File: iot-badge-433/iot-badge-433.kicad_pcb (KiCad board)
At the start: 2 copper layers, 70 x 100 mm, 72 parts, among them J1 USB_C_Receptacle_USB2.0, J2 Wire ANT, J3 Conn_01x04_Male, Q1 BC847, Q2 BC847, SW1 SW_Push, SW2 SW_Push, SW3 SW_Push, SW4 SW_Push, SW5 SW_Push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

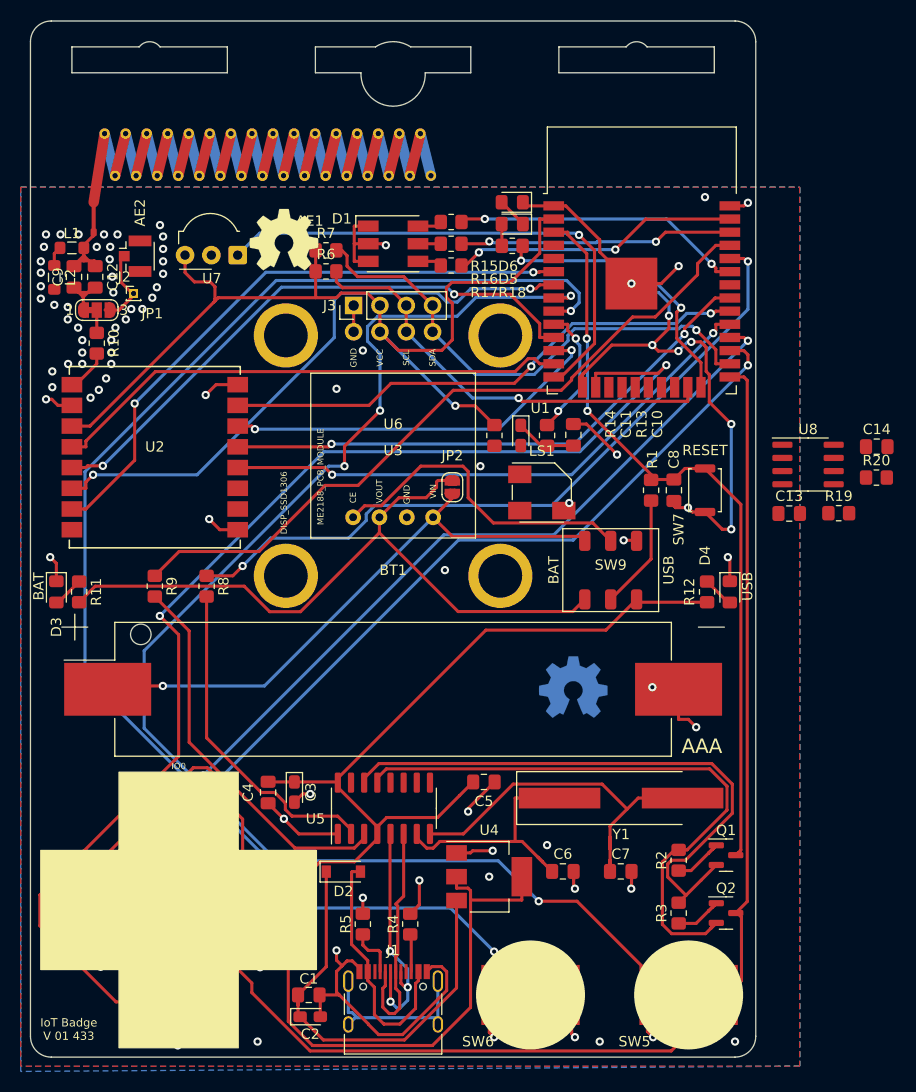
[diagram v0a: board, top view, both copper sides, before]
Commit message: audio amp elements routed
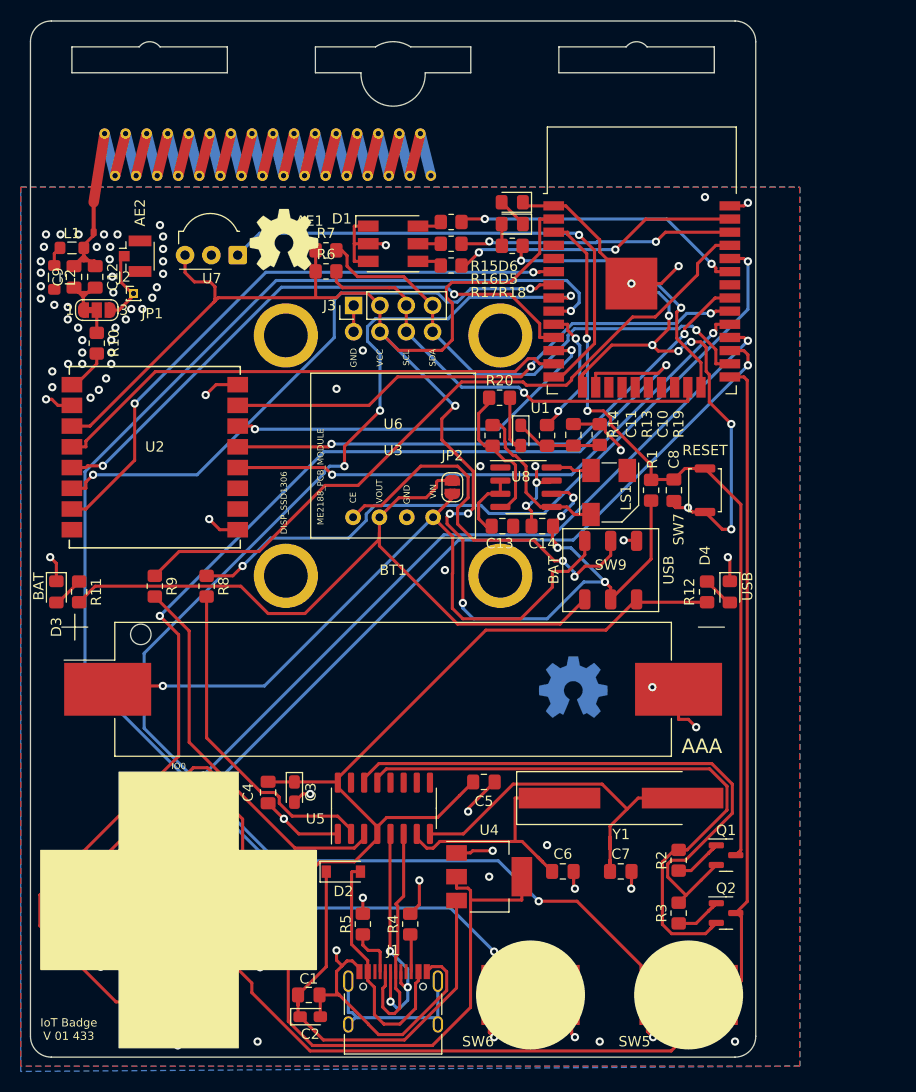
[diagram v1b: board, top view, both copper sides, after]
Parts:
- moved R20 37.2 mm to (145.3, 86.4)
- moved C14 33.2 mm to (149.4, 98.8), turned to 180 degrees
- moved C13 27.7 mm to (145.6, 98.8)
- moved U8 27.3 mm to (147.8, 95.0)
- moved R19 24.3 mm to (154.9, 89.9), turned to -90 degrees
- moved LS1 6.50 mm to (155.8, 95.5), turned to -90 degrees
- moved R14 0.18 mm to (144.6, 90.0)
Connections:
- LS1 pad 2: Net-(LS1-Pad2) -> Net-(U8-Pad8)
- LS1 pad 3: Net-(LS1-Pad3) -> Net-(R14-Pad1)
- R14 pad 1: Net-(LS1-Pad2) -> Net-(R14-Pad1)
- U8 pad 5: Net-(LS1-Pad2) -> Net-(R14-Pad1)
- U8 pad 8: Net-(LS1-Pad3) -> Net-(U8-Pad8)
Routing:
- net +3V3: track 103.3 -> 154.5 mm, vias 1 -> 8
- net Net-(R14-Pad1): track 0.00 -> 15.6 mm
- net Net-(R14-Pad2): track 0.00 -> 14.2 mm
- net +BATT: track 56.9 -> 68.9 mm
- net Earth: track 198.8 -> 207.1 mm, vias 96 -> 99
- net Net-(C13-Pad1): track 0.00 -> 6.81 mm
- net Net-(SW9-Pad5): track 31.4 -> 37.9 mm, vias 0 -> 2
- net Net-(C11-Pad2): track 0.00 -> 5.32 mm
- net Net-(U8-Pad8): track 0.00 -> 3.92 mm
- net Net-(C10-Pad1): track 5.91 -> 8.47 mm
- net Net-(JP2-Pad2): track 67.6 -> 69.8 mm
- net Net-(AE2-Pad1): track 8.27 -> 7.35 mm
- net /EN: track 73.7 -> 74.6 mm
- net Net-(R8-Pad1): track 69.8 -> 70.4 mm
- net /SDA: track 51.4 -> 50.8 mm
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
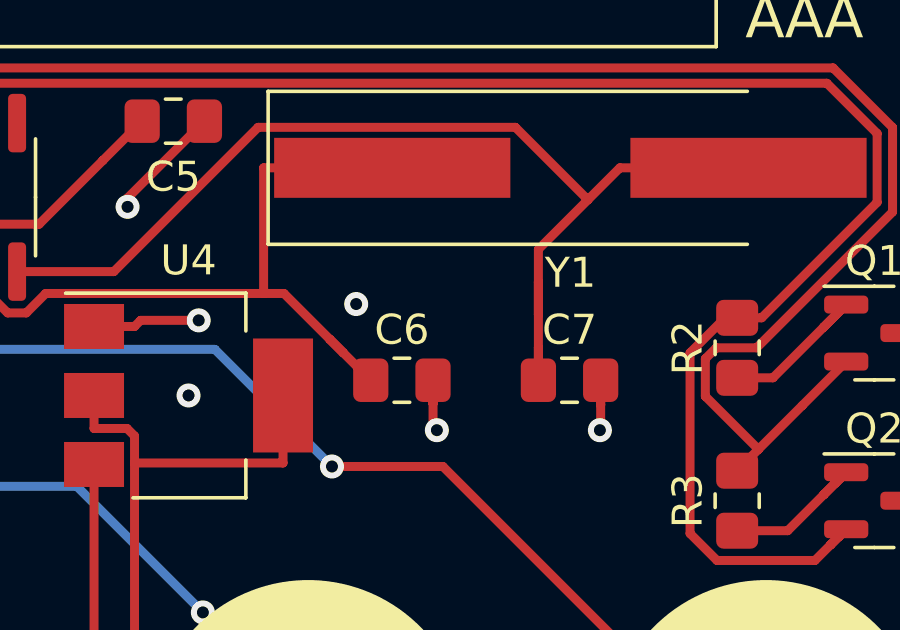
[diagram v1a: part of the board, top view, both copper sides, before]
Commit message: moved xtal capacitors to make some room
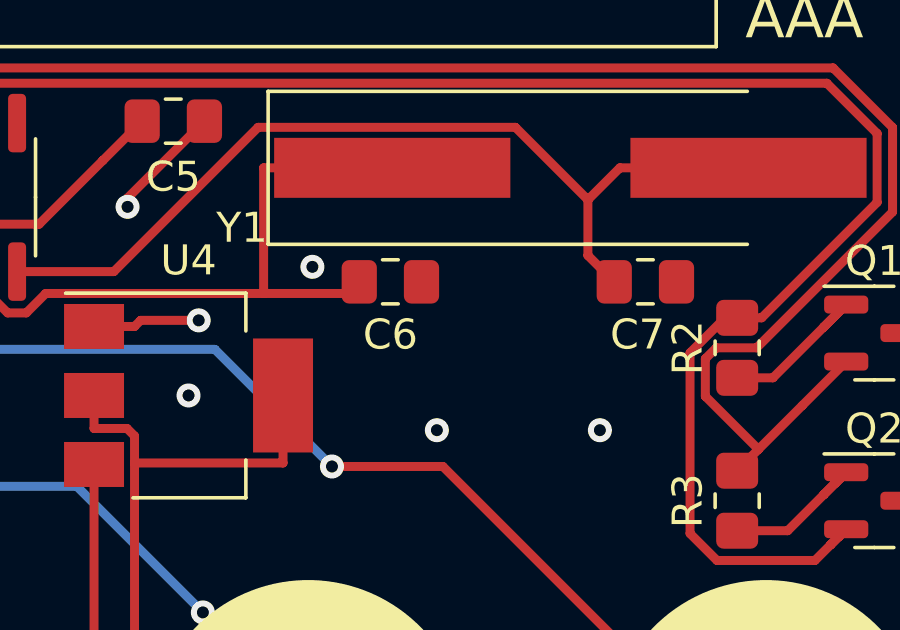
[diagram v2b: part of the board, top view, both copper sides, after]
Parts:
- moved C7 4.14 mm to (159.5, 128.8)
- moved C6 3.30 mm to (151.0, 128.8)
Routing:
- net Net-(C7-Pad1): track 36.7 -> 30.9 mm
- net Earth: track 207.1 -> 202.1 mm
- net Net-(C6-Pad1): track 25.1 -> 22.4 mm

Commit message: added resistors to sw to protect against shorts
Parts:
- added R21: 220, Resistor_SMD:R_0805_2012Metric_Pad1.20x1.40mm_HandSolder, F.Cu at (156.9, 141.0)
- added R22: 220, Resistor_SMD:R_0805_2012Metric_Pad1.20x1.40mm_HandSolder, F.Cu at (154.9, 141.0)
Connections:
- SW5 pad 1: /SW5-32 -> Net-(SW5-Pad1)
- SW6 pad 1: /SW6-33 -> Net-(SW6-Pad1)
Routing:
- net Net-(SW6-Pad1): track 0.00 -> 11.4 mm
- net /SW5-32: track 138.4 -> 127.6 mm
- net Net-(SW5-Pad1): track 0.00 -> 10.7 mm

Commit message: moved capacitors to make room
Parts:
- moved C4 2.38 mm to (125.3, 124.2)
- moved C3 2.23 mm to (127.7, 124.2)
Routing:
- net +3.3VP: track 132.3 -> 130.1 mm
- net Earth: track 202.1 -> 201.2 mm
- net Net-(R8-Pad2): track 32.0 -> 32.6 mm

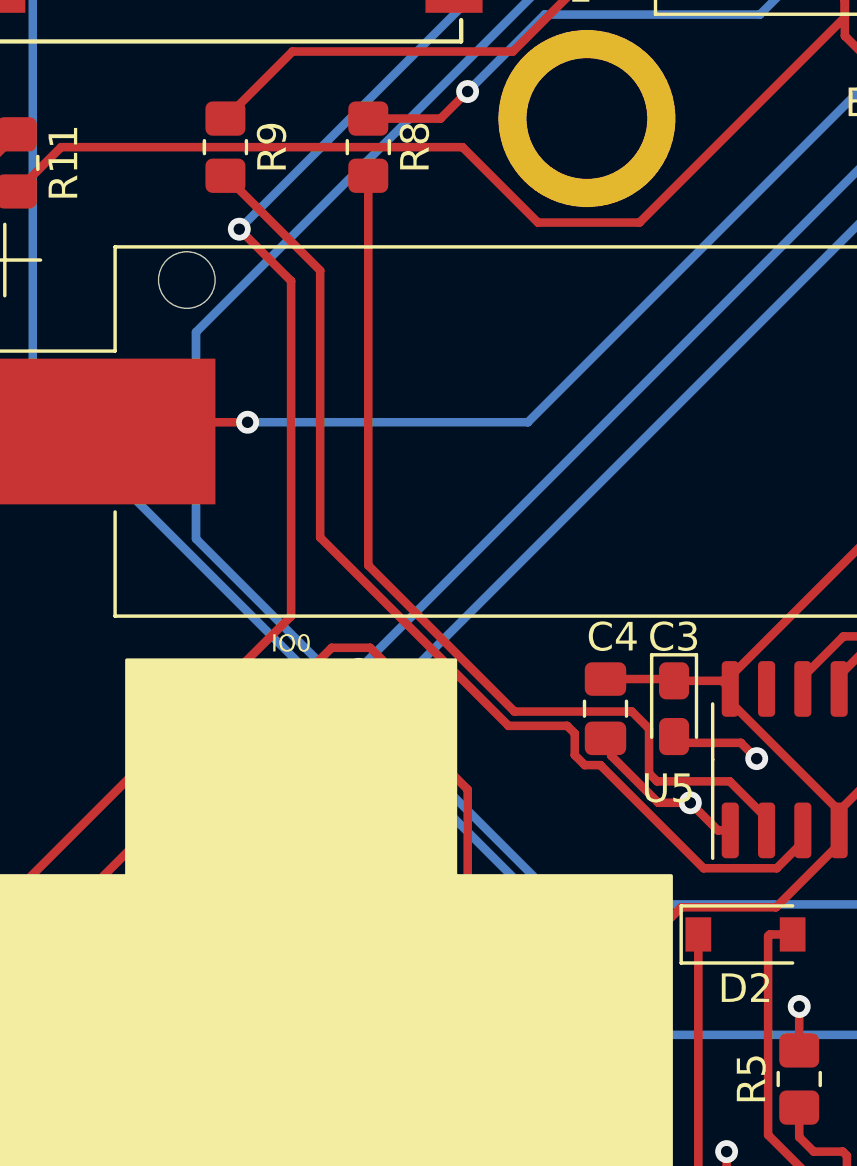
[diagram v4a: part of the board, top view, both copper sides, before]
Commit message: added resistor to switch
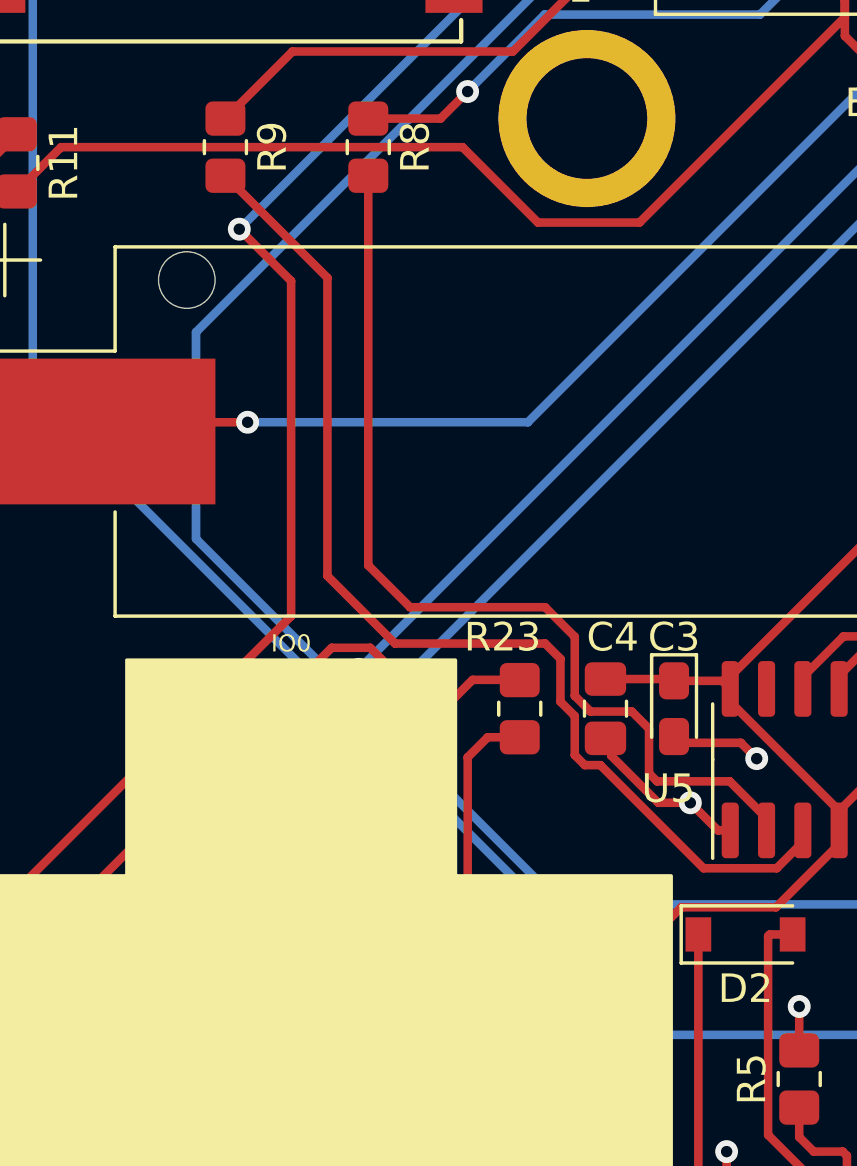
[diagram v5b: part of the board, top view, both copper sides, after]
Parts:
- added R23: 220, Resistor_SMD:R_0805_2012Metric_Pad1.20x1.40mm_HandSolder, F.Cu at (122.3, 124.2)
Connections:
- SW4 pad 1: /SW4-17 -> Net-(SW4-Pad1)
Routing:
- net Net-(SW4-Pad1): track 0.00 -> 20.1 mm
- net /SW4-17: track 94.5 -> 78.9 mm
- net Net-(R9-Pad2): track 37.0 -> 38.8 mm
- net Net-(R8-Pad2): track 32.6 -> 33.8 mm

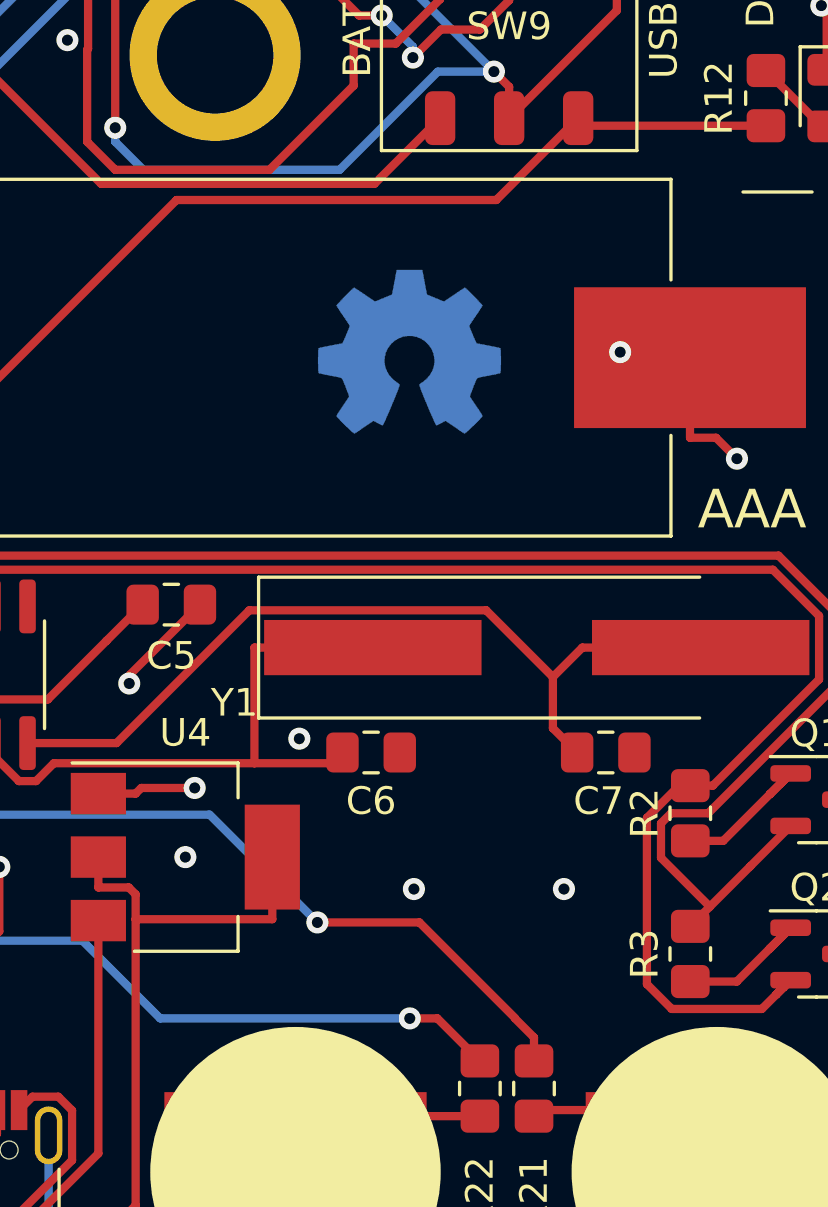
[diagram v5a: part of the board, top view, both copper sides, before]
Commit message: placed i2c mic in pcb
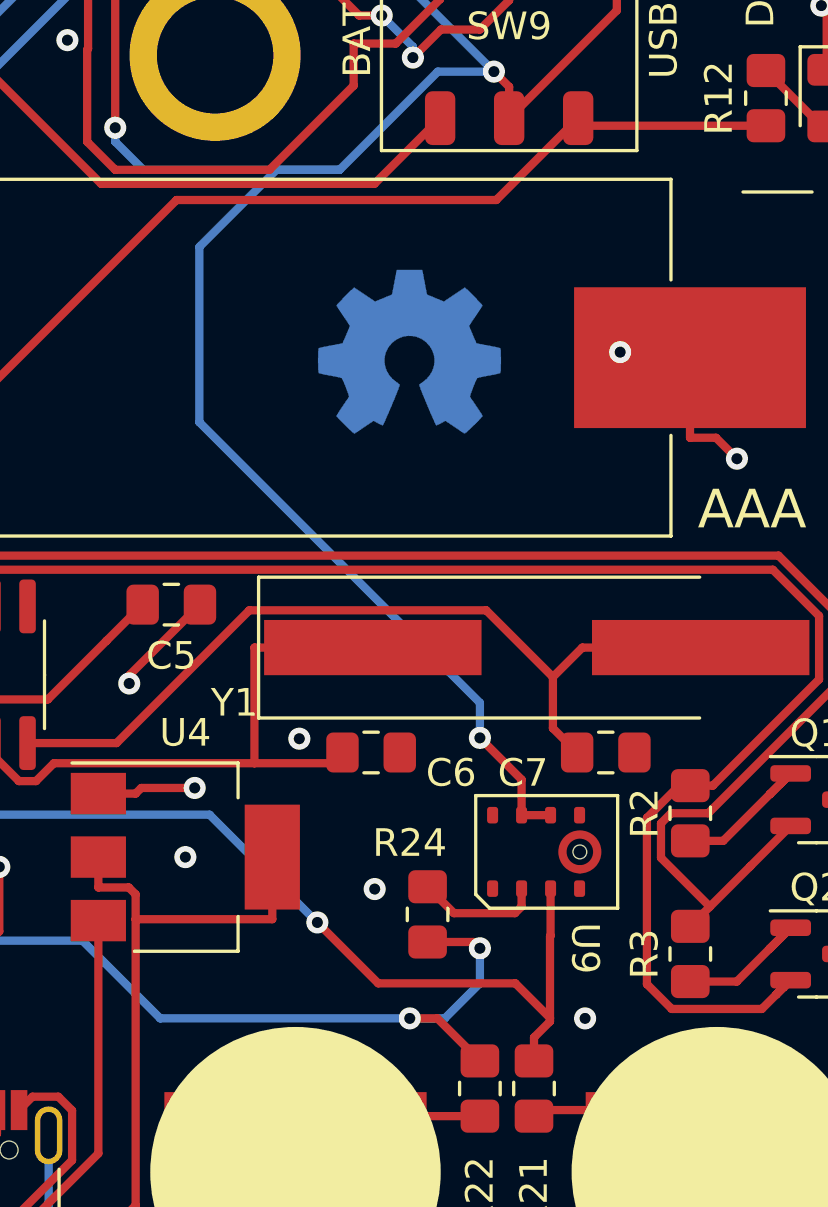
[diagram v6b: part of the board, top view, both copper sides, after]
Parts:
- added R24: 2,2K, Resistor_SMD:R_0805_2012Metric_Pad1.20x1.40mm_HandSolder, F.Cu at (153.0, 134.7)
- added U9: INMP441, Microphone_I2S:INMP441, F.Cu at (157.5, 132.4)
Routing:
- net +3V3: track 154.5 -> 187.2 mm, vias 8 -> 9
- net /SW6-33: track 140.1 -> 146.4 mm, vias 2 -> 3
- net /SW5-32: track 127.6 -> 133.5 mm
- net Net-(U9-Pad2): track 0.00 -> 4.55 mm

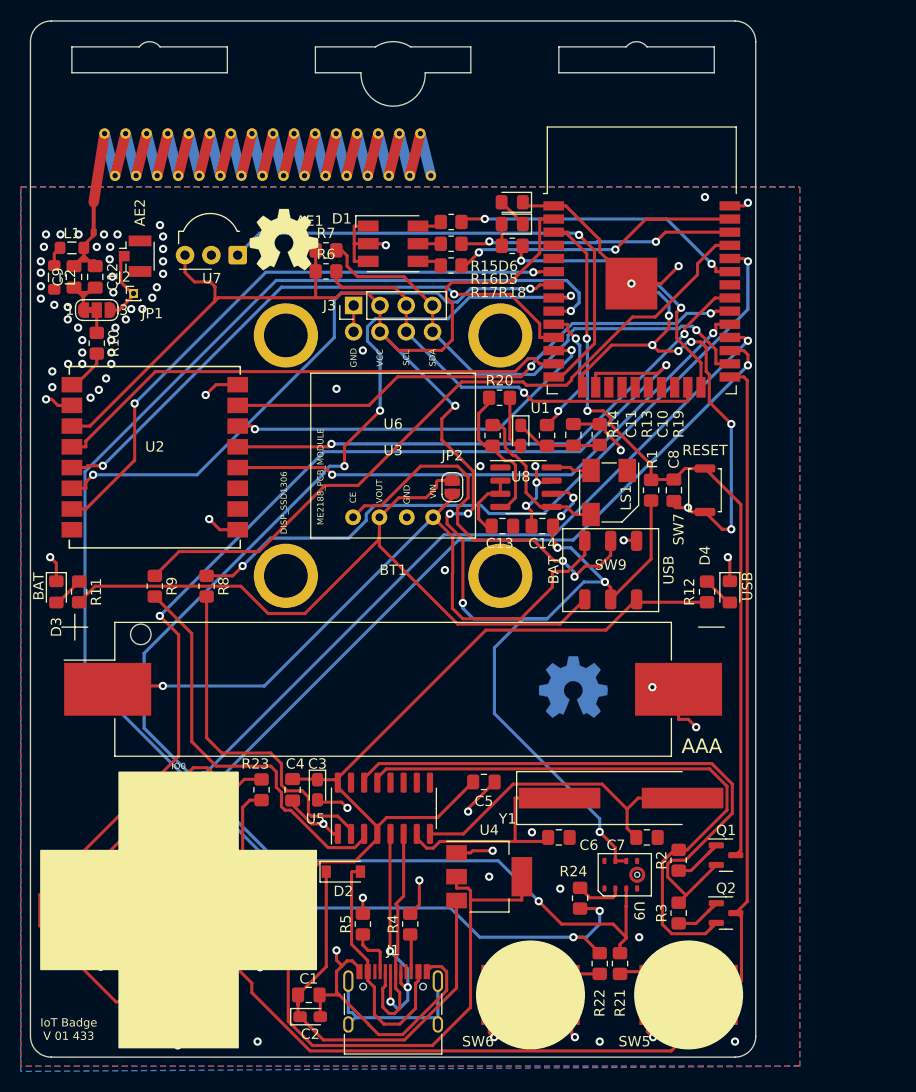
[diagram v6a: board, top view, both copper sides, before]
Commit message: finished placing i2s mic
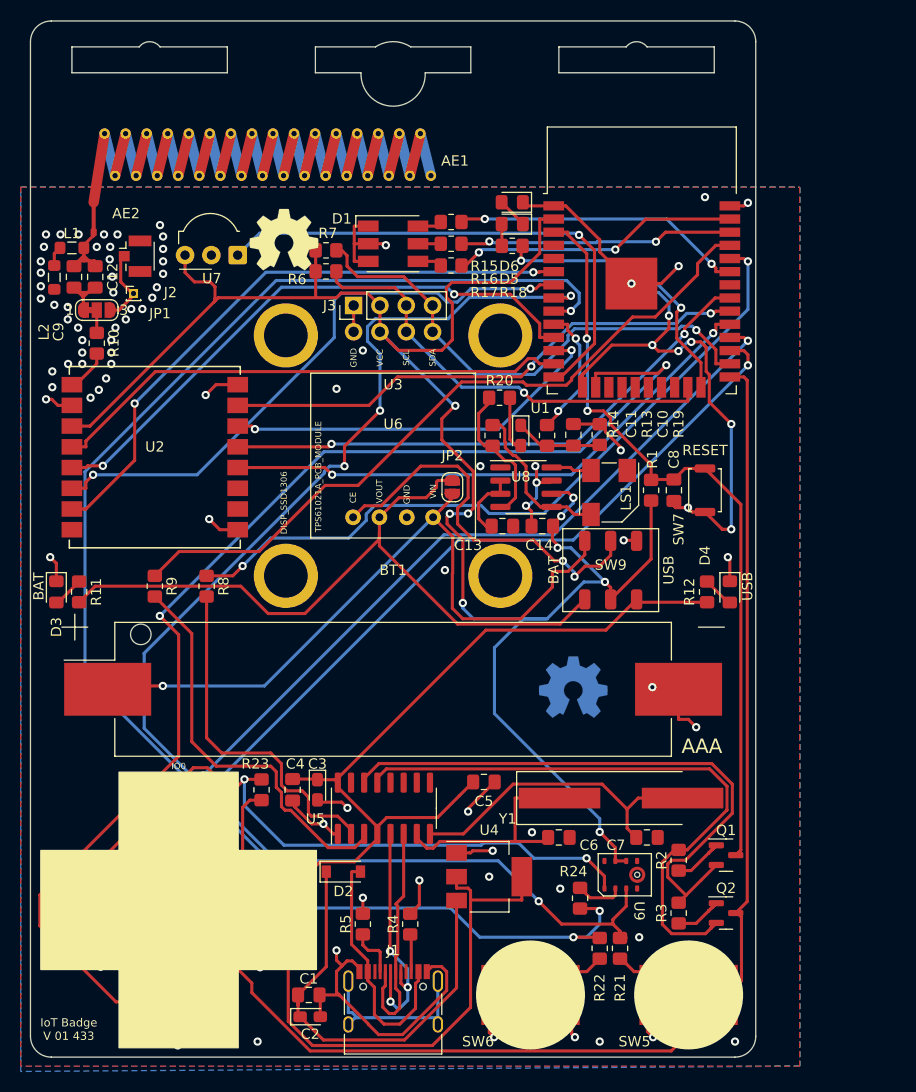
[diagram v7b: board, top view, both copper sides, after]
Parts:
- moved R21 1.47 mm to (156.9, 139.5)
- moved R22 1.47 mm to (154.9, 139.5)
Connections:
- U9 pad 1: unconnected-(U9-Pad1) -> /SW4-17
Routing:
- net /SW4-17: track 78.9 -> 120.4 mm, vias 2 -> 4
- net /SW5-32: track 133.5 -> 130.9 mm
- net Net-(R22-Pad1): track 11.4 -> 12.1 mm
- net /SW6-33: track 146.4 -> 145.8 mm
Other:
- board text added: "TPS61021A_PCB_MODULE"
- board text removed: "ME2188_PCB_MODULE"
